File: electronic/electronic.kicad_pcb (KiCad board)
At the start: 2 copper layers, 64.5 x 63 mm, 16 parts, among them J1 M_PWM, J10 BMP01, J11 MPU6050_01, J12 NEO_06_01, J14 OLED, J15 HCSR01, J16 HCSR02, J17 HCSR03, J18 HCSR04, J2 BAT_AX, J20 25.5-24 ESP32, U10 DEVKIT_V1_ESP32-WROOM-32, U6 DHT22

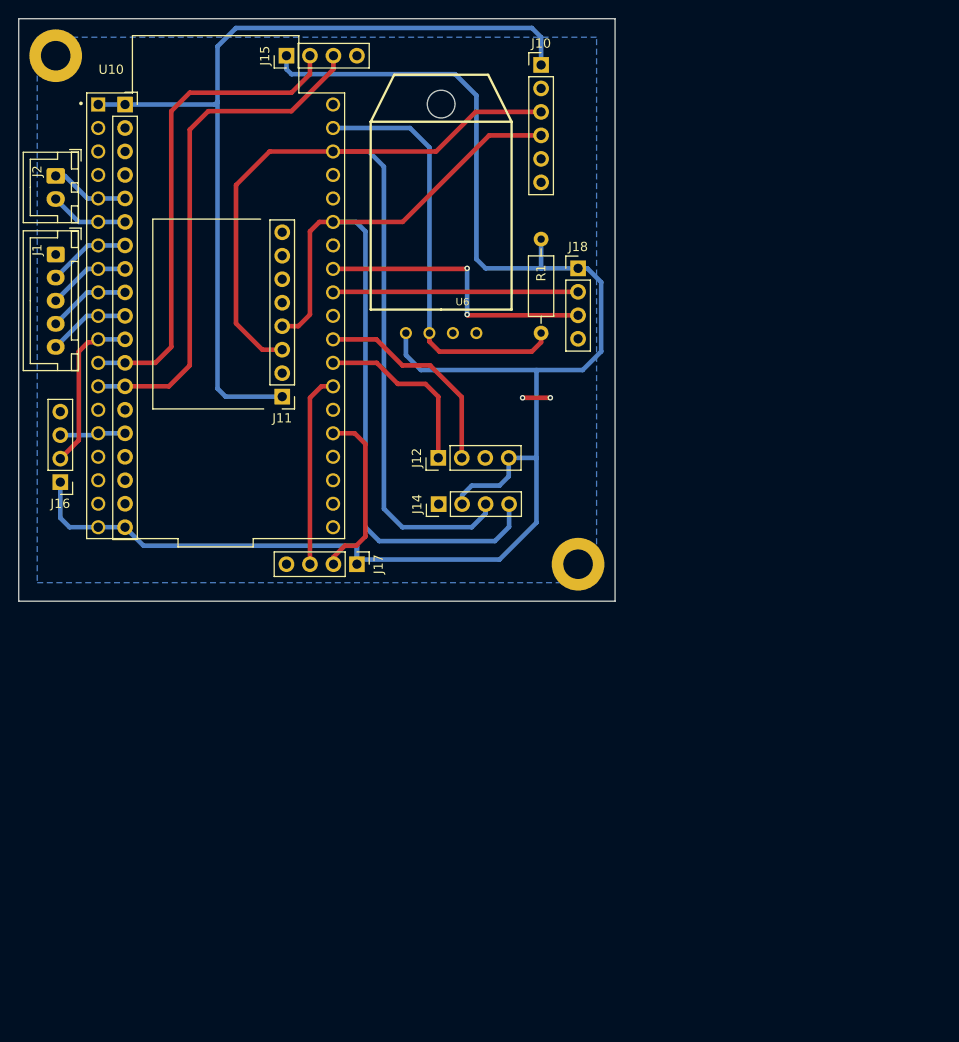
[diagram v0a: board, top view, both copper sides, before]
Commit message: feat (electronic): Unify electronic and power PCBs into one
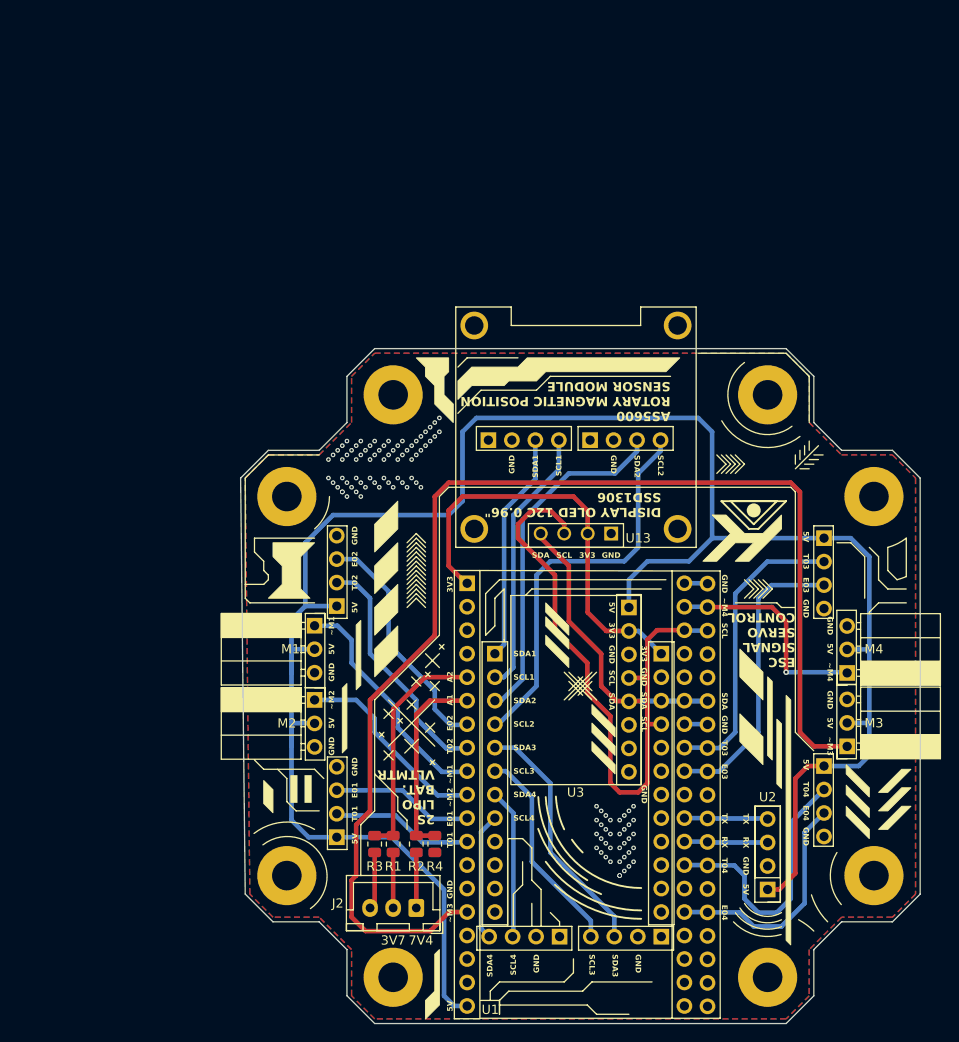
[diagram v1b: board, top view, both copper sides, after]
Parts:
- removed J1: M_PWM, Connector_JST:JST_XH_B5B-XH-A_1x05_P2.50mm_Vertical
- removed J10: BMP01, Connector_PinHeader_2.54mm:PinHeader_1x06_P2.54mm_Vertical
- removed J11: MPU6050_01, Connector_PinHeader_2.54mm:PinHeader_1x08_P2.54mm_Vertical
- removed J12: NEO_06_01, Connector_PinHeader_2.54mm:PinHeader_1x04_P2.54mm_Vertical
- removed J14: OLED, Connector_PinHeader_2.54mm:PinHeader_1x04_P2.54mm_Vertical
- removed J15: HCSR01, Connector_PinHeader_2.54mm:PinHeader_1x04_P2.54mm_Vertical
- removed J16: HCSR02, Connector_PinHeader_2.54mm:PinHeader_1x04_P2.54mm_Vertical
- removed J17: HCSR03, Connector_PinHeader_2.54mm:PinHeader_1x04_P2.54mm_Vertical
- removed J18: HCSR04, Connector_PinHeader_2.54mm:PinHeader_1x04_P2.54mm_Vertical
- removed J20: 25.5-24 ESP32, Connector_PinSocket_2.54mm:PinSocket_1x19_P2.54mm_Vertical
- removed the REF** at (18.5, 18.3)
- removed the REF** at (75.0, 73.3)
- removed U10: DEVKIT_V1_ESP32-WROOM-32, custom:MODULE_DEVKIT_V1_ESP32-WROOM-32
- removed U6: DHT22, custom:DHT22
- added IC1: AS5600-ASOT, Connector_PinSocket_2.54mm:PinSocket_1x04_P2.54mm_Horizontal, B.Cu at (65.3, 59.9)
- added IC2: AS5600-ASOT, Connector_PinSocket_2.54mm:PinSocket_1x04_P2.54mm_Horizontal, B.Cu at (76.3, 59.9)
- added IC3: AS5600-ASOT, Connector_PinSocket_2.54mm:PinSocket_1x04_P2.54mm_Horizontal, B.Cu at (84.0, 113.6)
- added IC4: AS5600-ASOT, Connector_PinSocket_2.54mm:PinSocket_1x04_P2.54mm_Horizontal, B.Cu at (73.0, 113.6)
- added M1: ESC, Connector_PinSocket_2.54mm:PinSocket_1x03_P2.54mm_Horizontal, F.Cu at (46.5, 80.0)
- added M2: ESC, Connector_PinSocket_2.54mm:PinSocket_1x03_P2.54mm_Horizontal, F.Cu at (46.5, 88.0)
- added M3: ESC, Connector_PinSocket_2.54mm:PinSocket_1x03_P2.54mm_Horizontal, F.Cu at (104.1, 93.0)
- added M4: ESC, Connector_PinSocket_2.54mm:PinSocket_1x03_P2.54mm_Horizontal, F.Cu at (104.1, 85.1)
- added R2: 390k, Resistor_SMD:R_0805_2012Metric, F.Cu at (57.5, 103.6)
- added R3: 100k, Resistor_SMD:R_0805_2012Metric, F.Cu at (53.0, 103.6)
- added R4: 100k, Resistor_SMD:R_0805_2012Metric, F.Cu at (59.5, 103.6)
- added REF**: MountingHole_3.2mm_M3_Pad, MountingHole:MountingHole_3.2mm_M3_Pad, F.Cu at (55.0, 55.0)
- added REF**: MountingHole_3.2mm_M3_Pad, MountingHole:MountingHole_3.2mm_M3_Pad, F.Cu at (55.0, 118.0)
- added REF**: MountingHole_3.2mm_M3_Pad, MountingHole:MountingHole_3.2mm_M3_Pad, F.Cu at (107.0, 107.0)
- added REF**: MountingHole_3.2mm_M3_Pad, MountingHole:MountingHole_3.2mm_M3_Pad, F.Cu at (107.0, 66.0)
- added REF**: MountingHole_3.2mm_M3_Pad, MountingHole:MountingHole_3.2mm_M3_Pad, F.Cu at (95.5, 55.0)
- added REF**: MountingHole_3.2mm_M3_Pad, MountingHole:MountingHole_3.2mm_M3_Pad, F.Cu at (43.5, 66.0)
- added REF**: MountingHole_3.2mm_M3_Pad, MountingHole:MountingHole_3.2mm_M3_Pad, F.Cu at (43.5, 107.0)
- added REF**: MountingHole_3.2mm_M3_Pad, MountingHole:MountingHole_3.2mm_M3_Pad, F.Cu at (95.5, 118.0)
- added U1: ESP32-DEVKITC-V4, local:MODULE_ESP32-DEVKITC-V4, F.Cu at (76.0, 98.1)
- added U13: SSD1306, local:MODULE_DM-OLED096-636, F.Cu at (74.8, 58.5)
- added U15: HC-SR04, Connector_PinSocket_2.54mm:PinSocket_1x04_P2.54mm_Horizontal, B.Cu at (48.9, 102.8)
- added U16: HC-SR04, Connector_PinSocket_2.54mm:PinSocket_1x04_P2.54mm_Horizontal, B.Cu at (48.9, 77.8)
- added U17: HC-SR04, Connector_PinSocket_2.54mm:PinSocket_1x04_P2.54mm_Horizontal, B.Cu at (101.6, 70.5)
- added U18: HC-SR04, Connector_PinSocket_2.54mm:PinSocket_1x04_P2.54mm_Horizontal, B.Cu at (101.6, 95.2)
- added U2: NEO-6M-GPS, Connector_PinHeader_2.54mm:PinHeader_1x04_P2.54mm_Vertical, F.Cu at (95.5, 108.5)
- added U3: MPU-9250+BMP280, local:MPU9250, F.Cu at (74.7, 86.7)
- added U4: TCA9548AMRGER, local:TCA9548A, B.Cu at (75.0, 96.7)
- J2: footprint Connector_JST:JST_XH_B2B-XH-A_1x02_P2.50mm_Vertical -> Connector_JST:JST_XH_B3B-XH-A_1x03_P2.50mm_Vertical
- R1: value 10k -> 390k; footprint Resistor_THT:R_Axial_DIN0207_L6.3mm_D2.5mm_P10.16mm_Horizontal -> Resistor_SMD:R_0805_2012Metric
- moved J2 88.3 mm to (57.5, 110.5), turned to 180 degrees
- moved R1 67.4 mm to (55.0, 103.6), turned to 90 degrees
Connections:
- J2 pad 1: A01 -> Net-(J2-Pin_1)
- J2 pad 2: A02 -> Net-(J2-Pin_2)
- R1 pad 1: +5V -> Net-(J2-Pin_2)
- R1 pad 2: DHT_SIG -> A02
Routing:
- net M3_SIGN: track 0.00 -> 135.5 mm
- net BMP_SCK01: track 114.0 -> 0.00 mm
- net BMP_SDI01: track 97.0 -> 0.00 mm
- net IMU_SCL: track 0.00 -> 71.8 mm
- net ULTRAE01: track 56.0 -> 0.00 mm
- net ULTRAT01: track 52.8 -> 0.00 mm
- net +3.3V: track 96.6 -> 45.9 mm
- net DHT_SIG: track 46.2 -> 0.00 mm
- net +5V: track 181.2 -> 225.7 mm
- net SW_CL02: track 0.00 -> 43.1 mm
- net IMU_SDA: track 0.00 -> 39.4 mm
- net SW_DA02: track 0.00 -> 37.9 mm
- net CH_T03: track 0.00 -> 32.3 mm
- net CH_E03: track 0.00 -> 32.0 mm
- net ULTRAE04: track 31.6 -> 0.00 mm, vias 2 -> 0
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- added copper zone on F.Cu, net Earth
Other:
- board size 64.5 x 63 mm -> 73.5 x 73 mm
- board text added: "2S LIPO BAT. VLTMTR"
- board text added: "3V3"
- board text added: "3V7"
- board text added: "5V"
- board text added: "7V4"
- board text added: "A1"
- board text added: "A2"
- board text added: "AK VANT II"
- board text added: "AS5600 ROTARY MAGNETIC POSITION SENSOR MODULE"
- board text added: "DISPLAY OLED 12C 0.96{dblquote} SSD1306"
- board text added: "E01"
- board text added: "E02"
- board text added: "E03"
- board text added: "E04"
- board text added: "ESC SIGNAL SERVO CONTROL"
- board text added: "GND"
- board text added: "II"
- board text added: "J2"
- board text added: "R1"
- board text added: "R2"
- board text added: "R3"
- board text added: "R4"
- board text added: "RX"
- board text added: "SCL"
- board text added: "SCL1"
- board text added: "SCL2"
- board text added: "SCL3"
- board text added: "SCL4"
- board text added: "SDA"
- board text added: "SDA1"
- board text added: "SDA2"
- board text added: "SDA3"
- board text added: "SDA4"
- board text added: "T01"
- board text added: "T02"
- board text added: "T03"
- board text added: "T04"
- board text added: "TX"
- board text added: "~M1"
- board text added: "~M2"
- board text added: "~M3"
- board text added: "~M4"
